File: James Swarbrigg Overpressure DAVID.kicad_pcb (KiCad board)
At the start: 2 copper layers, 130 x 98 mm, 20 parts, among them J1 Screw_Terminal_01x02, J2 Screw_Terminal_01x02, J3 Fuse Holder 200mA, J4 Screw_Terminal_01x02, K1 G5V-2, Q1 BC184L, U2 TSR_1-2450, U3 LM358N

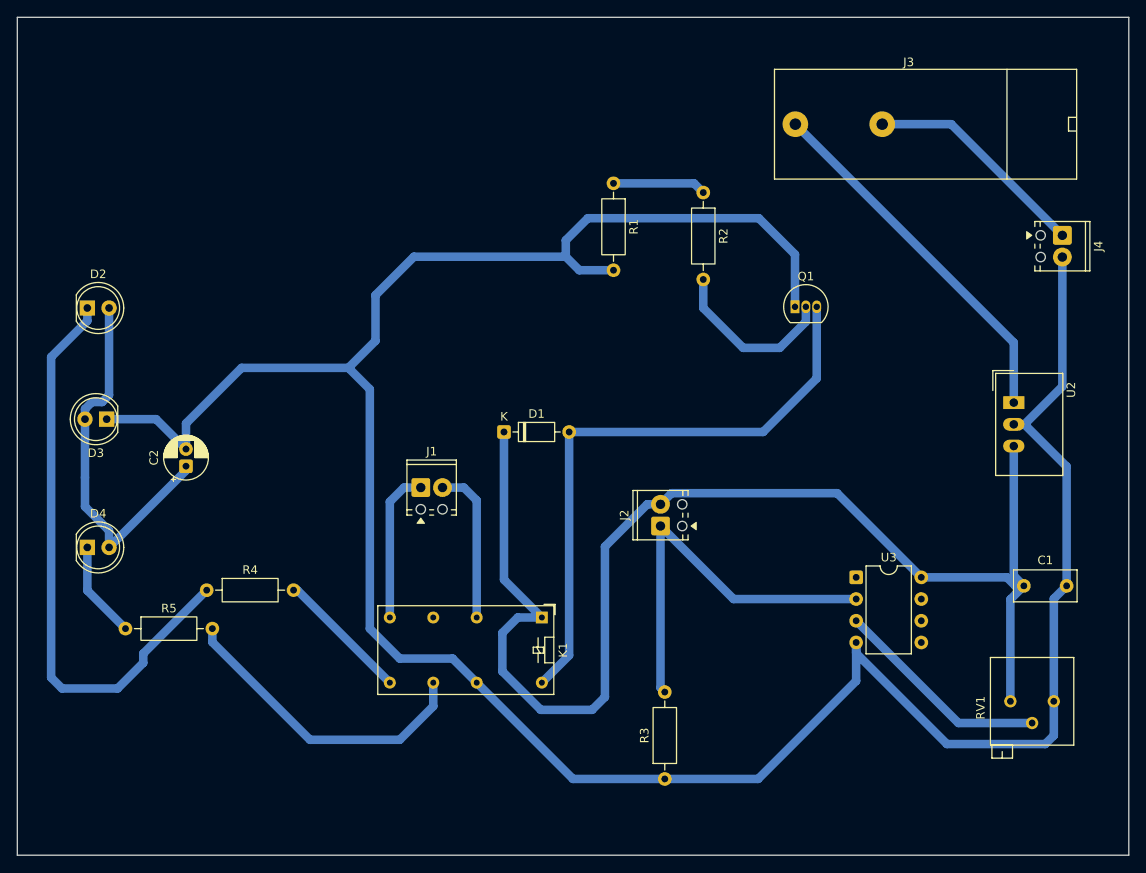
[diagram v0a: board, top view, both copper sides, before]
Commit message: Update overpressure cutout PCB and add Gerbers V1
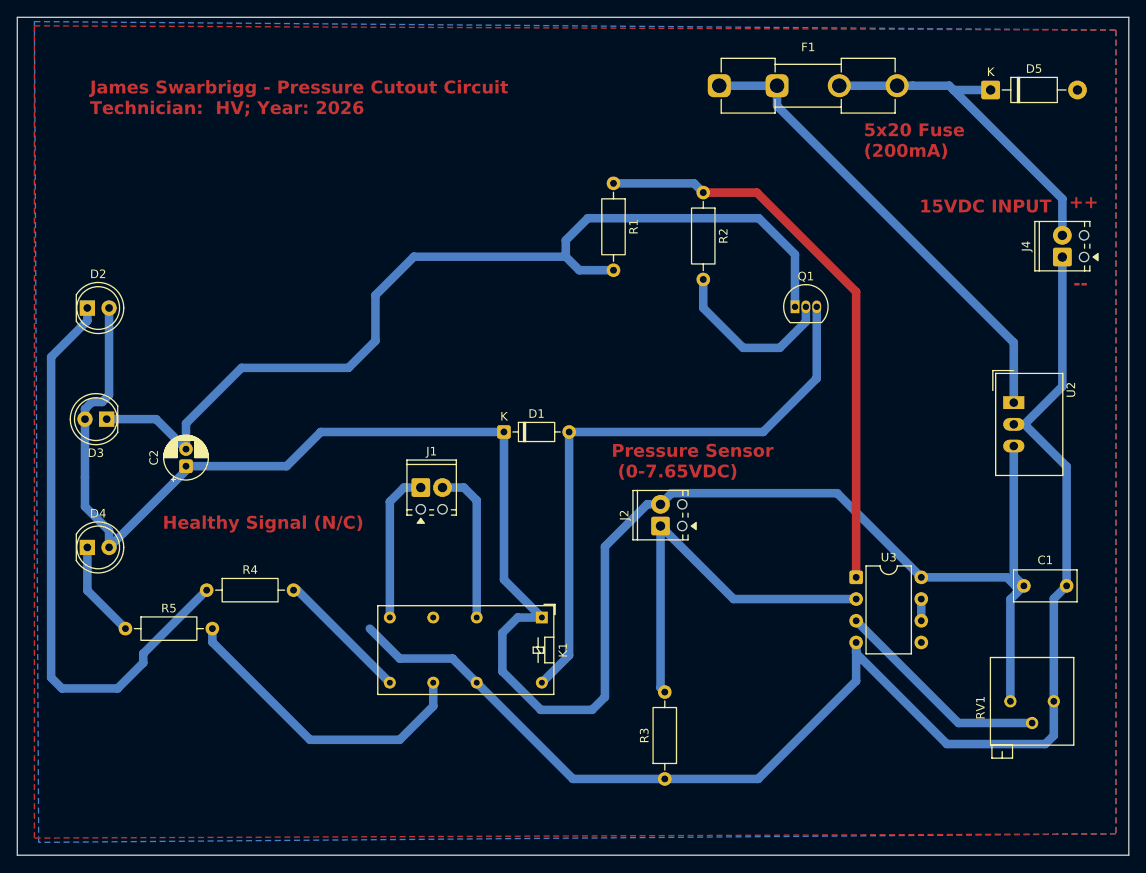
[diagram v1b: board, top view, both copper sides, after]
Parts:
- removed J3: Fuse Holder 200mA, Fuse:Fuseholder_Cylinder-5x20mm_Bulgin_FX0457_Horizontal_Closed
- added D5: 1N4001, Diode_THT:D_DO-41_SOD81_P10.16mm_Horizontal, F.Cu at (188.8, 46.5)
- added F1: Fuse, Fuse:Fuseholder_Clip-5x20mm_Eaton_1A5601-01_Inline_P20.80x6.76mm_D1.70mm_Horizontal, F.Cu at (157.1, 46.0)
- moved J4 2.54 mm to (197.2, 66.0), turned to 90 degrees
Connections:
- J4 pad 1: Net-(J3-Pin_2) -> GND
- J4 pad 2: GND -> Net-(D5-K)
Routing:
- net Net-(R1-Pad1): track 10.9 -> 67.0 mm
- net Net-(D5-K): track 0.00 -> 40.2 mm
- net +5V: track 196.8 -> 235.7 mm
- net GND: track 309.1 -> 277.6 mm
- net Net-(J3-Pin_2): track 26.5 -> 0.00 mm
- net Net-(U2-Vin): track 43.1 -> 55.3 mm
- net Net-(U3B--): track 0.00 -> 2.54 mm
- added copper zone on B.Cu, net GND
- added copper zone on F.Cu, net GND
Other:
- board text added: "++"
- board text added: "--"
- board text added: "15VDC INPUT"
- board text added: "5x20 Fuse (200mA)"
- board text added: "Healthy Signal (N/C)"
- board text added: "James Swarbrigg - Pressure Cutout Circuit Technician: HV; Year: 2026"
- board text added: "Pressure Sensor (0-7.65VDC)"
